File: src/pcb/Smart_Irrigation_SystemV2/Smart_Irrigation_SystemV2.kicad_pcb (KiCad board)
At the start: 4 copper layers, 100 x 55.5 mm, 128 parts, among them CN1 PJ-3136-3A, CN2 PJ-3136-3A, CN3 PJ-3136-3A, CN4 PJ-3136-3A, CN5 PJ-3136-3A, CN6 PJ-3136-3A, J1 USB_C_Receptacle_USB2.0_16P, J14 SolarPanel, J15 I2C, J16 GPIO_Expander, J9 Battary Connection, Q1 MUN5211DW1, Q2 FDN340P, Q3 AO3400A, SW1 IO0 Switch, SW2 EN Switch, SW3 SW_Push, SW4 SW_Push, SW5 SW_Push, SW6 SW_Push, U1 CP2102N-Axx-xQFN28, U10 ADS1115IDGS, U11 PCA9536DP, U2 ESP32-WROOM-32, U3 ADS1115IDGS, U4 DS3231MZ, U5 TLV62568ADRL, U6 SN74LVC245APW, U7 TP4056-42-ESOP8, U8 TPS63001

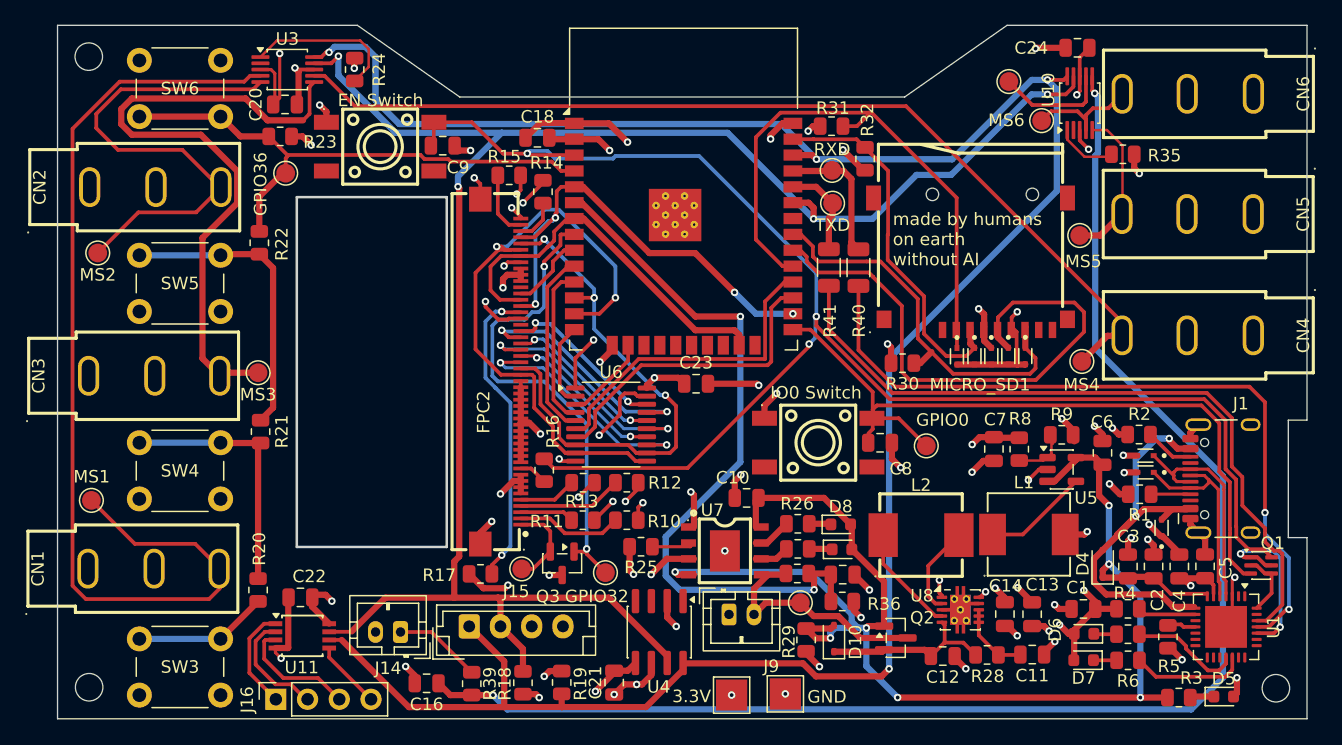
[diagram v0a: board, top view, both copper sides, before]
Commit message: 3d printed a scaled model of it, had to move the USBC closer to edge, rerouted, made hole for fpc wider, saved 40$ while placing all components on one side, time spend for this commit: 2h
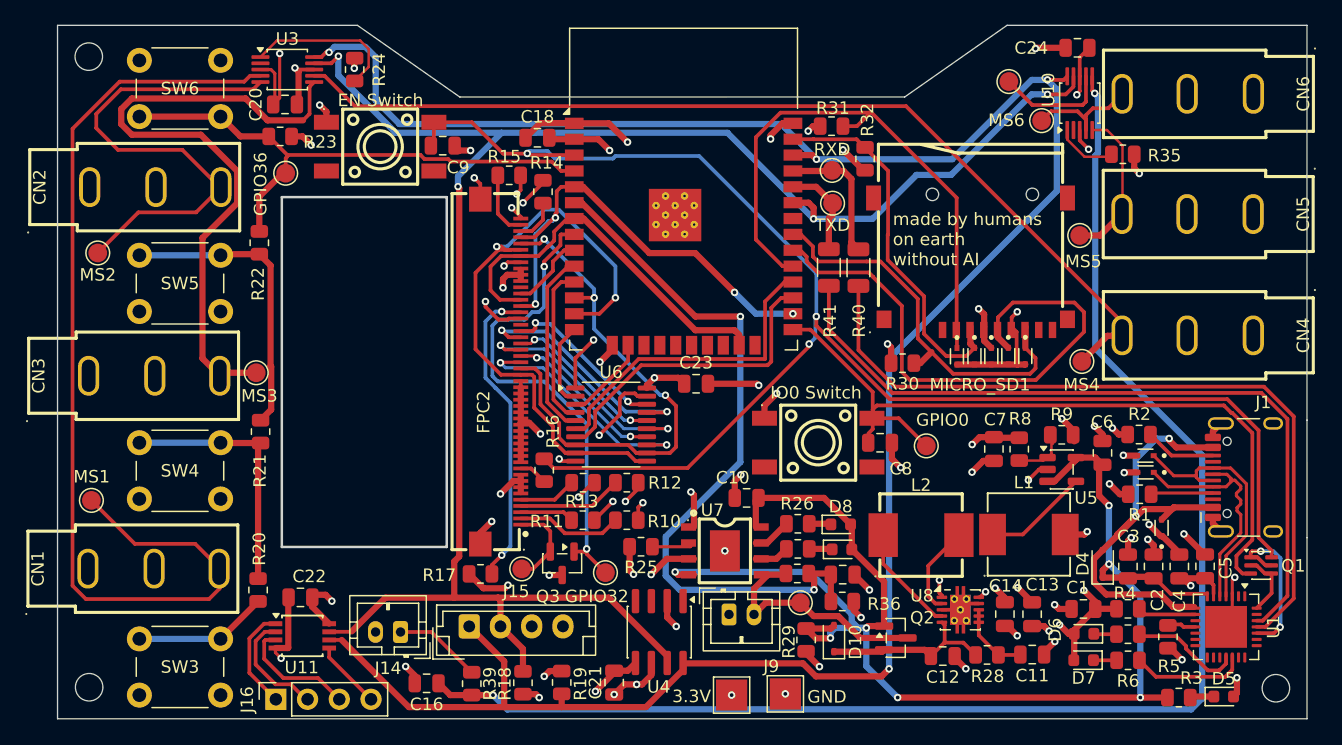
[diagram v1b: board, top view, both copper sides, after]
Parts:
- moved J1 1.80 mm to (178.6, 112.6)
- moved TP8 0.15 mm to (98.2, 104.2)
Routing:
- net /D-: track 16.4 -> 19.7 mm
- net /VBUS_IN: track 34.4 -> 37.2 mm
- net /D+: track 17.4 -> 20.1 mm
- net /TXD: track 58.1 -> 60.6 mm
- net /GPIO0: track 59.1 -> 61.3 mm
- net Net-(J1-CC1): track 2.90 -> 4.99 mm
- net Net-(J1-CC2): track 3.93 -> 5.69 mm
- net /RTS: track 14.0 -> 12.6 mm
- net /SolarPanel: track 120.4 -> 119.0 mm
- net /RXD: track 59.9 -> 60.7 mm, vias 2 -> 0
- net GND: track 153.8 -> 154.3 mm, vias 54 -> 55
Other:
- outline, holes or cut-outs redrawn
